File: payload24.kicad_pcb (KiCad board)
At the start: 4 copper layers, 89.4 x 89.4 mm, 21 parts, among them J1 532540370, J3 460150206, J4 532540370, Q1 CSD19503KCS, Q2 CSD19503KCS, SW1 FingerTech

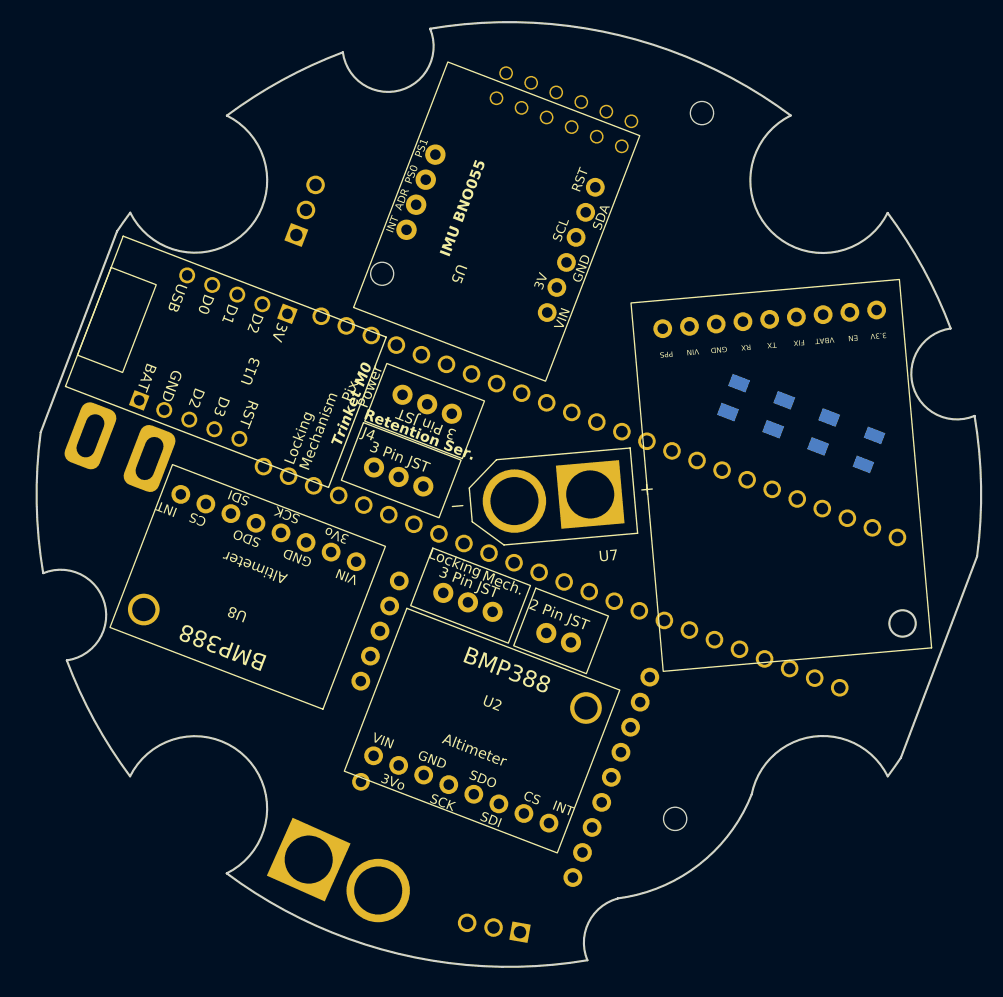
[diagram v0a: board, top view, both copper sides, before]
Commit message: PCB layer and power setup
Made PCB 6-Layers
Routed .1in power connection
Setup power plane thermal relief spoke width and gap
Moved Mosfet, power regular, and other components around a little
Rotated PCB 21 degrees
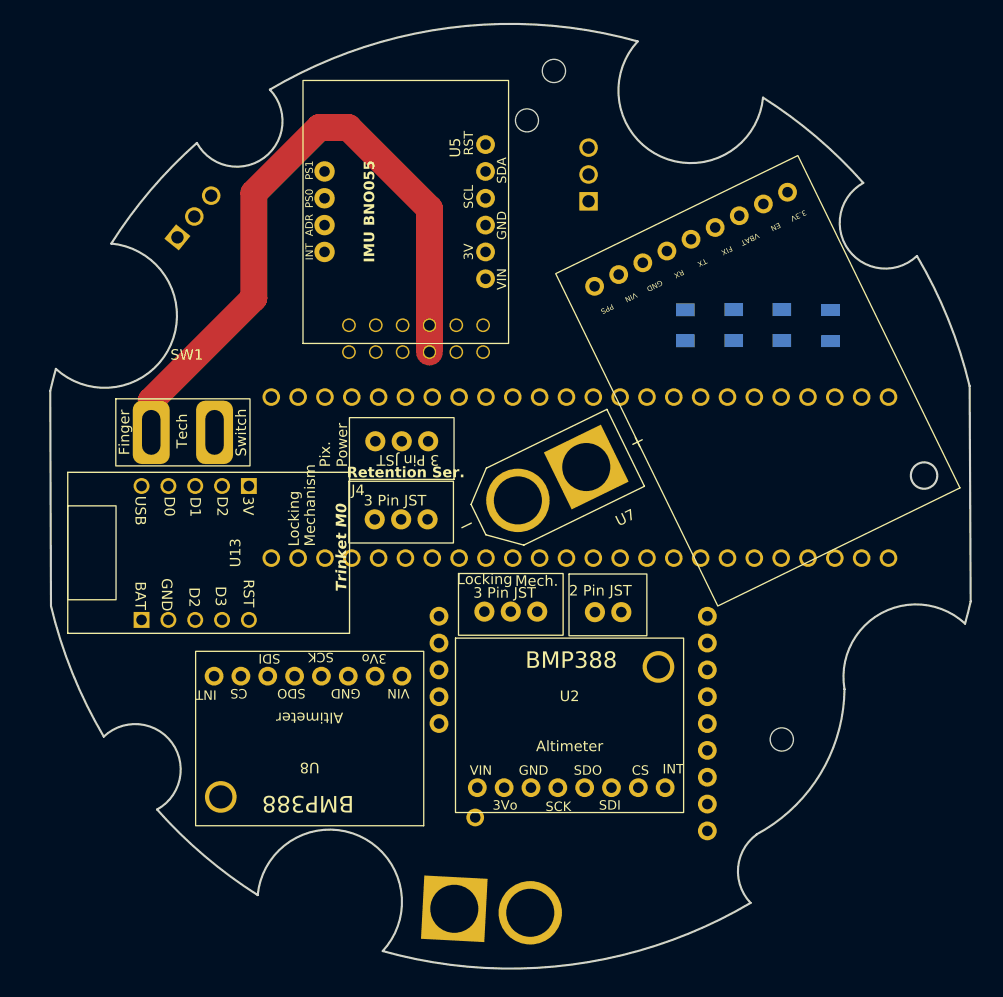
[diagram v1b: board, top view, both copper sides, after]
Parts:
- SW1: moved to F.Cu
- moved Q1 71.8 mm to (72.0, 29.6), turned to 90 degrees
- moved U5 26.0 mm to (68.4, 22.3), turned to 180 degrees
- moved U13 18.2 mm to (36.0, 65.5), turned to -90 degrees
- moved U8 16.0 mm to (45.6, 85.3), turned to 180 degrees
- moved U3 15.4 mm to (107.2, 59.3), turned to -154 degrees
- moved U6 14.5 mm to (62.9, 99.3), turned to -3 degrees
- moved R1 12.3 mm to (94.9, 44.0), turned to 90 degrees
- moved R2 10.9 mm to (90.3, 43.9), turned to 90 degrees
- moved Q2 10.6 mm to (34.7, 33.6), turned to 51 degrees
- moved R3 9.50 mm to (85.7, 43.9), turned to 90 degrees
- moved SW1 8.50 mm to (27.3, 50.9), turned to 0 degrees
- moved R4 8.23 mm to (81.2, 43.9), turned to 90 degrees
- moved U14 8.20 mm to (54.6, 34.4), turned to 90 degrees
- moved U4 7.86 mm to (70.7, 80.4), turned to -90 degrees
- moved U2 7.50 mm to (70.2, 79.5), turned to 0 degrees
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- renumbered Je to J2
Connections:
- net Net-(SW1-A) renamed /.1in
- net Net-(SW1-B) renamed /22.2V
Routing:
- net /.1in: track 0.00 -> 62.6 mm
- added copper zone on In4.Cu, net /22.2V
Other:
- board size 89.4 x 89.4 mm -> 87.1 x 89.4 mm
- copper layers 4 -> 6

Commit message: update (1/7/24)
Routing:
- net RST3: track 0.00 -> 124.8 mm, vias 0 -> 1
- net GND - NMOS2: track 0.00 -> 93.6 mm
- net Net-(Q2-Pad1): track 0.00 -> 76.0 mm, vias 0 -> 7
- net Power Signal: track 0.00 -> 68.9 mm
- net SDA3: track 0.00 -> 67.4 mm
- net 3.3V-Teensy: track 0.00 -> 66.4 mm, vias 0 -> 1
- net RX1: track 0.00 -> 55.1 mm, vias 0 -> 3
- net SCL3: track 0.00 -> 49.3 mm, vias 0 -> 1
- net TX1: track 0.00 -> 47.6 mm, vias 0 -> 3
- net RST2: track 0.00 -> 46.7 mm, vias 0 -> 3
- net 3.3V-Teensy1: track 0.00 -> 46.4 mm, vias 0 -> 4
- net GND - NMOS1: track 0.00 -> 46.0 mm, vias 0 -> 2
- net MOSI: track 0.00 -> 42.4 mm
- net MISO: track 0.00 -> 38.3 mm, vias 0 -> 2
- net 3.3V-Trinket: track 0.00 -> 37.5 mm
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- added copper zone on In3.Cu, net GND - NMOS1

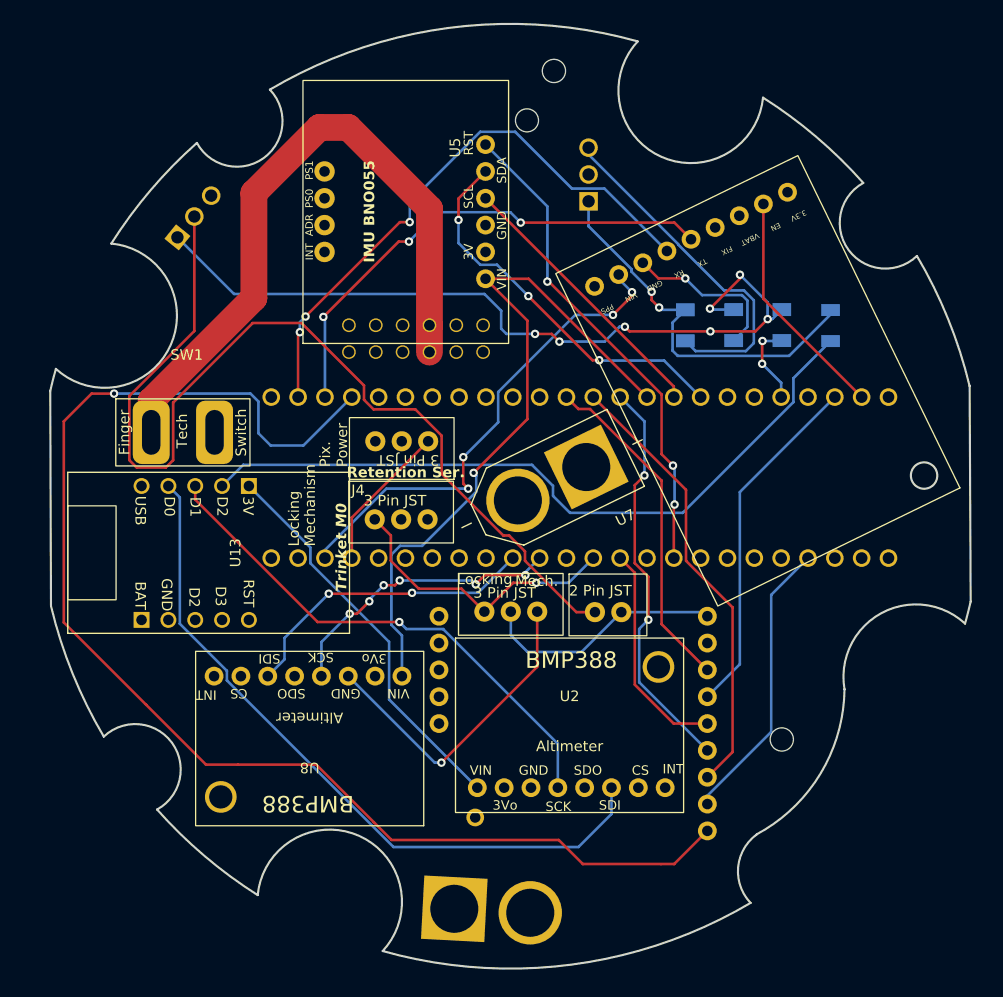
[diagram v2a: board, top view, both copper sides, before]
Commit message: updated pcb
uploading unsaved changes
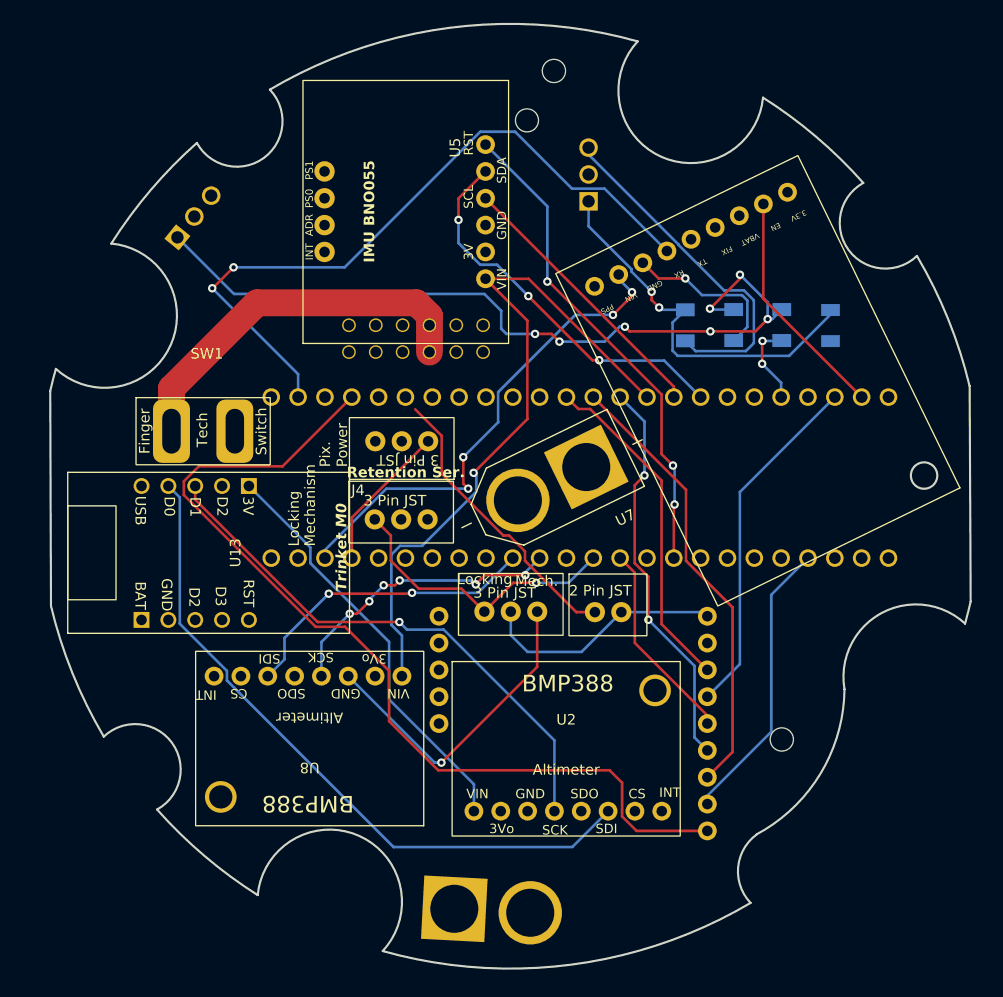
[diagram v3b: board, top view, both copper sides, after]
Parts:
- moved U2 2.25 mm to (69.9, 81.8)
- moved SW1 1.92 mm to (29.2, 50.8)
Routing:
- net Power Signal: track 68.9 -> 0.00 mm
- net GND - NMOS2: track 93.6 -> 27.6 mm
- net TX1: track 47.6 -> 0.00 mm, vias 3 -> 0
- net RST3: track 124.8 -> 87.9 mm, vias 1 -> 0
- net /.1in: track 62.6 -> 35.8 mm
- net RX1: track 55.1 -> 67.8 mm, vias 3 -> 2
- net SDA3: track 67.4 -> 64.7 mm
- net 3.3V-Trinket: track 37.5 -> 39.6 mm
- net SCL3: track 49.3 -> 51.4 mm
- net SCK: track 21.0 -> 19.1 mm
- net MISO: track 38.3 -> 37.6 mm

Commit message: Update payload24.kicad_pcb
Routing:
- net Power Signal: track 0.00 -> 64.6 mm
- net TX1: track 0.00 -> 42.3 mm, vias 0 -> 1
- net GND - NMOS2: track 27.6 -> 66.0 mm
- net MISO: track 37.6 -> 45.4 mm
- net unconnected-(U5-VRP-Pad3): track 0.00 -> 2.54 mm
- net 3.3V-Teensy1: track 46.4 -> 43.9 mm, vias 4 -> 2
- net GND: track 33.3 -> 31.9 mm
- net SCL1: track 27.7 -> 29.1 mm, vias 6 -> 2
- net Net-(Q2-Pad1): track 76.0 -> 77.3 mm, vias 7 -> 2
- net SDA1: track 29.0 -> 27.9 mm
- net /Open Signal: vias 1 -> 0

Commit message: final updates prior to purchasing (1/17)
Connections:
- Q2 pad 3: GND - NMOS1 -> GND
- R3 pad 1: GND - NMOS1 -> GND
- U1 pad 29: Altitude Signal -> unconnected-(U1-PWM|TX7-Pad29)
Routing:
- net GND - NMOS1: track 46.0 -> 40.7 mm, vias 2 -> 1
- net GND: track 31.9 -> 35.1 mm
- net Net-(Q2-Pad1): track 77.3 -> 79.6 mm
- net Net-(Q1-Pad1): track 37.2 -> 38.2 mm
- net SDA2: track 36.8 -> 37.7 mm
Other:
- outline, holes or cut-outs redrawn

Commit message: update
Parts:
- removed J1, J2, J4: 532540370, JST-XH3:JST-XH3
- removed J3: 460150206, JST-XH2:JST-XH2
- removed Q1, Q2: CSD19503KCS, teensyMosfet:teensyMosfet
- removed R1: 500, 500Ohm:RESC3216X65N
- removed R2: 1000, 1kOhm:RESC3216X70N
- removed R3, R4: 10K, 10KOhm:RESC3216X70N
- removed SW1: FingerTech, FingerTech:FingerTech
- removed U1: ~, Teensy:TEENSY41
- removed U13: ~, Trinket M0:Trinket M0
- removed U14: ~, BNO055:BNO055
- removed U2, U8: ~, BMP388:BMP388
- removed U3: ~, adafruit gps:GPS_adafruit
- removed U4: ~, RFModule:RFM_LoRa
- removed U5: ~, poluluRegulator:VoltageRegulator
- removed U6, U7: ~, XT60:AMASS_XT60-M
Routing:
- net RST3: track 87.9 -> 0.00 mm
- net Net-(Q2-Pad1): track 79.6 -> 0.00 mm, vias 2 -> 0
- net RX1: track 67.5 -> 0.00 mm, vias 2 -> 0
- net 3.3V-Teensy: track 66.4 -> 0.00 mm, vias 1 -> 0
- net GND - NMOS2: track 65.8 -> 0.00 mm
- net SDA3: track 64.7 -> 0.00 mm
- net Power Signal: track 64.6 -> 0.00 mm
- net SCL3: track 51.4 -> 0.00 mm, vias 1 -> 0
- net RST2: track 46.7 -> 0.00 mm, vias 3 -> 0
- net MISO: track 45.4 -> 0.00 mm, vias 2 -> 0
- net 3.3V-Teensy1: track 43.9 -> 0.00 mm, vias 2 -> 0
- net MOSI: track 42.4 -> 0.00 mm
- net TX1: track 42.3 -> 0.00 mm, vias 1 -> 0
- net GND - NMOS1: track 40.7 -> 0.00 mm, vias 1 -> 0
- net 3.3V-Trinket: track 39.6 -> 0.00 mm
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- removed copper zone on In4.Cu, net /22.2V
- removed copper zone on In2.Cu, net 5V-Power Reg.
- removed copper zone on In1.Cu, net GND
- removed copper zone on In3.Cu, net GND - NMOS1
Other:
- board size 87.1 x 89.4 mm -> 89.1 x 89.4 mm
- board text added: "BOTTOM"
- board text added: "TOP"
- board text removed: "Locking"
- board text removed: "Mech."
- board text removed: "Mechanism"
- board text removed: "Pix. Power"
- board text removed: "Retention Ser."

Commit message: PCB laid out
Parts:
- added J1: JST-XH3, JST-XH3:JST-XH3, F.Cu at (69.2, 54.2)
- added J2: PixHawk, JST-XH2:JST-XH2, F.Cu at (57.5, 54.2)
- added J3: Motors, JST-XH3:JST-XH4, F.Cu at (69.2, 60.5)
- added J4: Motors, JST-XH3:JST-XH4, F.Cu at (52.5, 60.5)
- added Q2: CSD19503KCS, teensyMosfet:teensyMosfet, B.Cu at (59.6, 74.6)
- added Q3: IRLB4132, teensyMosfet:teensyMosfet, B.Cu at (67.5, 76.9)
- added R2: 1000, 1kOhm:RESC3216X70N, B.Cu at (36.5, 57.1)
- added R3: 10K, 10KOhm:RESC3216X70N, B.Cu at (36.5, 60.4)
- added R5: 1000, 1kOhm:RESC3216X70N, B.Cu at (36.5, 63.8)
- added R6: 10K, 10KOhm:RESC3216X70N, B.Cu at (36.5, 67.1)
- added SW1: FingerTech, FingerTech:FingerTech, F.Cu at (76.9, 102.7)
- added U1: ~, Teensy:TEENSY41, B.Cu at (49.7, 52.8)
- added U14: ~, BNO055:BNO055, F.Cu at (35.5, 60.3)
- added U2: LMS1585ACT-3.3/NOPB, teensyMosfet:vRegulator, B.Cu at (65.3, 84.8)
- added U3: ~, adafruit gps:GPS_adafruit, F.Cu at (81.6, 27.2)
- added U4: ~, RFModule:RFM_LoRa, B.Cu at (65.2, 33.4)
- added U5: ~, poluluRegulator:VoltageRegulator, F.Cu at (72.0, 67.0)
- added U6: ~, XT60:AMASS_XT60-M, B.Cu at (64.0, 99.2)
- added U7: LMS1585ACT-3.3/NOPB, teensyMosfet:vRegulator, B.Cu at (57.4, 82.5)
- added U8: ~, BMP388:BMP388, F.Cu at (86.7, 77.2)
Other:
- board size 89.1 x 89.4 mm -> 81.9 x 89.4 mm
- board text removed: "BOTTOM"
- board text removed: "TOP"

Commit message: Updates to PCB
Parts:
- moved R2 23.0 mm to (40.7, 34.5)
- moved R3 22.7 mm to (40.6, 38.1)
- moved R5 22.4 mm to (40.7, 41.7)
- moved R6 22.1 mm to (40.7, 45.3)
- moved U8 1.84 mm to (85.2, 78.3)
- moved U6 0.40 mm to (64.4, 99.1)
- moved U2 0.11 mm to (65.2, 84.8)
- moved U7 0.07 mm to (57.3, 82.5)
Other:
- board text added: "+"
- board text added: "-"
- board text added: "3.3V"
- board text added: "3V"
- board text added: "3Vo"
- board text added: "ADR"
- board text added: "CS"
- board text added: "DC Motors"
- board text added: "EN"
- board text added: "FIX"
- board text added: "G0"
- board text added: "G1"
- board text added: "G2"
- board text added: "G3"
- board text added: "G4"
- board text added: "G5"
- board text added: "GND"
- board text added: "GPS Module"
- board text added: "INT"
- board text added: "MISO"
- board text added: "MOSI"
- board text added: "PPS"
- board text added: "PS0"
- board text added: "PS1"
- board text added: "Pix Hawk"
- board text added: "RST"
- board text added: "RX"
- board text added: "SCK"
- board text added: "SCL"
- board text added: "SDA"
- board text added: "SDO"
- board text added: "Servo"
- board text added: "TEENSY 4.1"
- board text added: "TX"
- board text added: "VBAT"
- board text added: "VIN"
